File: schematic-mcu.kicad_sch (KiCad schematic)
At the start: 25 parts, among them U5 USBLC6-2P6, U6 ESP32-S3FN8, Y1 Crystal_GND24

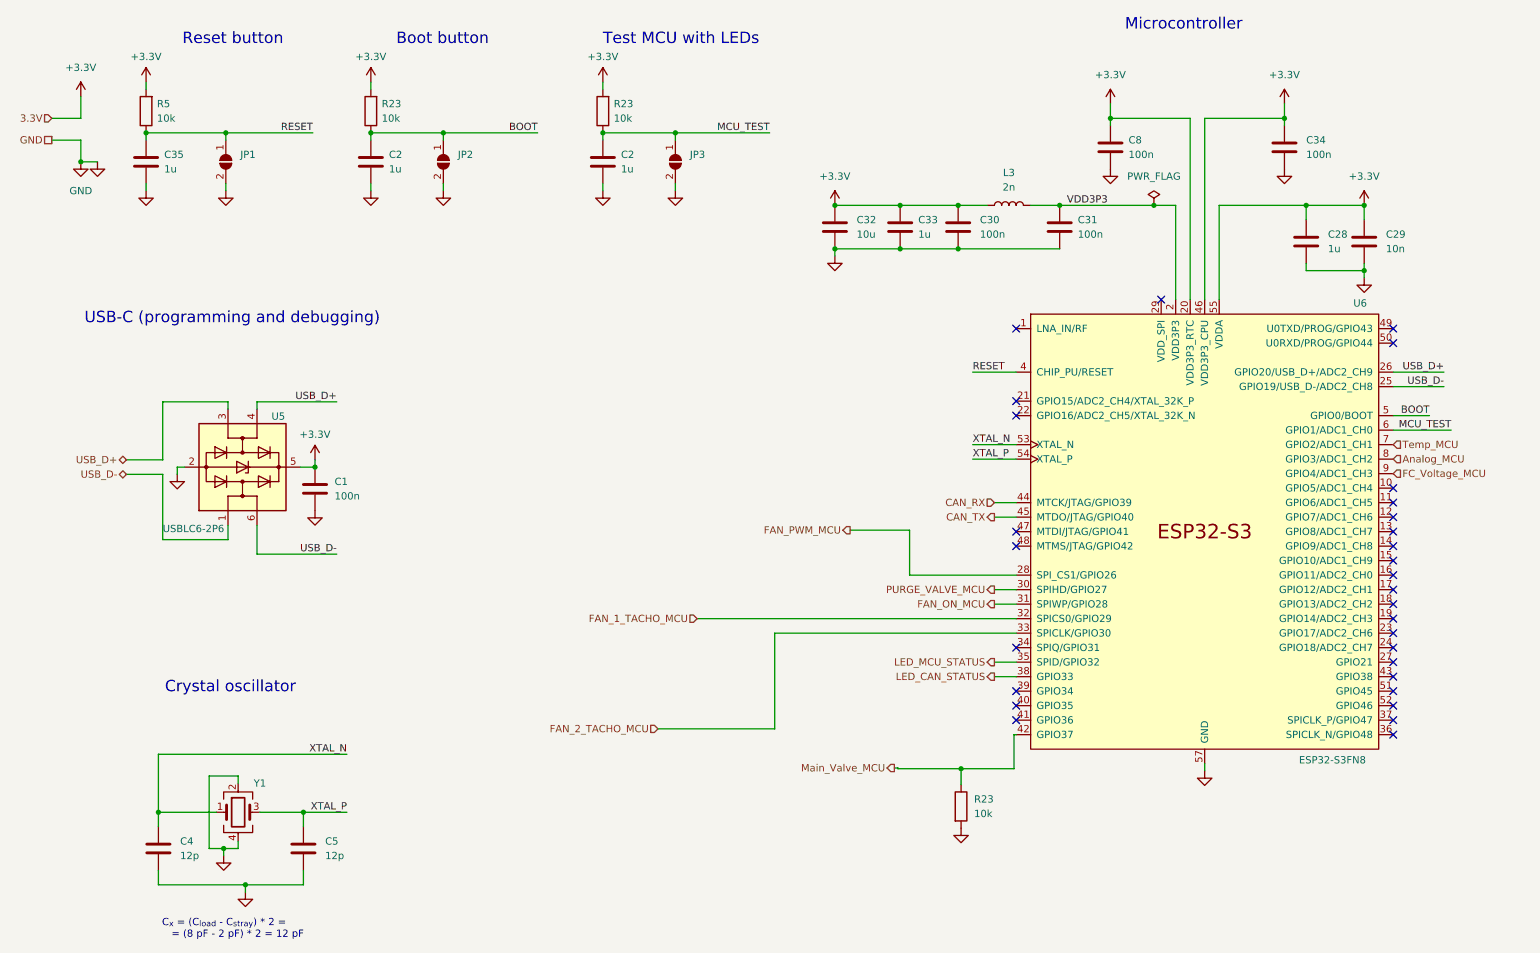
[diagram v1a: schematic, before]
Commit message: Edit mosfets outputs
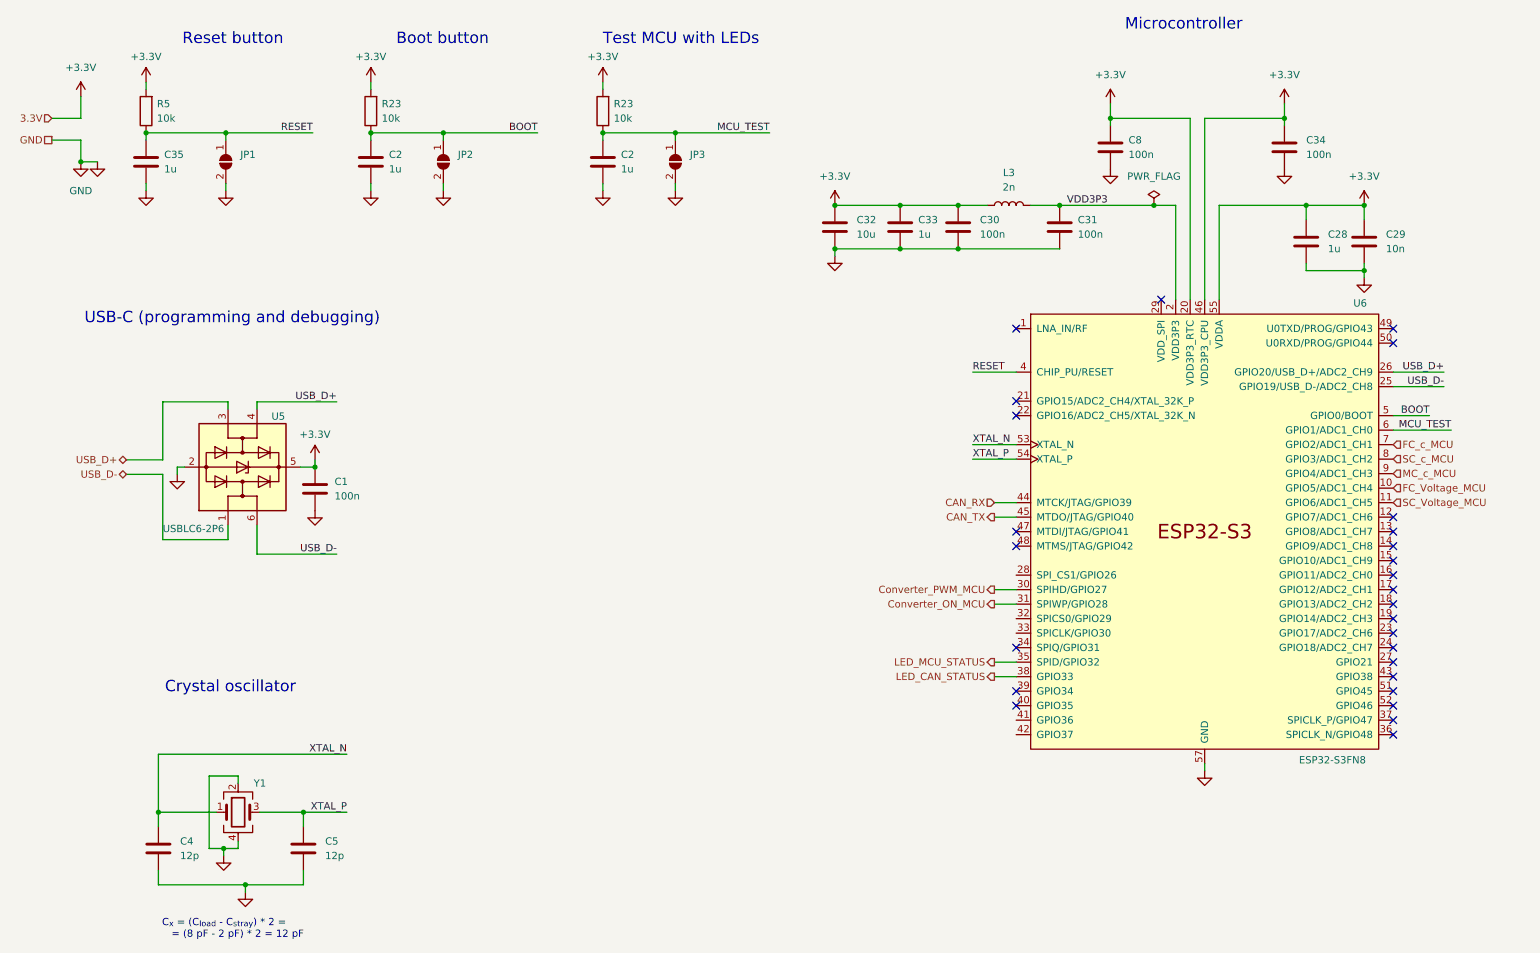
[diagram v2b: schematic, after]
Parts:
- removed R23: 10k, LED_SMD:LED_1206_3216Metric, symbol Device:R
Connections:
- net FC_Voltage_MCU: now also U6.10 (GPIO5/ADC1_CH4); no longer U6.9 (GPIO4/ADC1_CH3)
- net SC_Voltage_MCU: now reaches U6.11 (GPIO6/ADC1_CH5)
- net Analog_MCU renamed SC_c_MCU
- net FAN_1_TACHO_MCU: no longer names the net of U6.32 (SPICS0/GPIO29)
- net FAN_2_TACHO_MCU: no longer names the net of U6.33 (SPICLK/GPIO30)
- net FAN_ON_MCU renamed Converter_ON_MCU
- net FAN_PWM_MCU: no longer names the net of U6.28 (SPI_CS1/GPIO26)
- net Main_Valve_MCU: no longer names the net of U6.42 (GPIO37)
- net PURGE_VALVE_MCU renamed Converter_PWM_MCU
- net Temp_MCU renamed FC_c_MCU
- new net MC_c_MCU: U6.9 (GPIO4/ADC1_CH3)
- no-connect marks 30 -> 27
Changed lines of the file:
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@@
   (junction (at 185.42 53.34) (diameter 0) (color 0 0 0 0)
-  )
-  (junction (at 185.928 152.019) (diameter 0) (color 0 0 0 0)
   )
   (junction (at 31.75 45.72) (diameter 0) (color 0 0 0 0)
@@
   (no_connect (at 261.62 130.81))
   (no_connect (at 195.58 74.93))
-  (no_connect (at 261.62 102.87))
   (no_connect (at 195.58 138.43))
   (no_connect (at 261.62 118.11))
@@
   (no_connect (at 261.62 146.05))
   (no_connect (at 261.62 110.49))
-  (no_connect (at 195.58 143.51))
   (no_connect (at 195.58 110.49))
   (no_connect (at 261.62 135.89))
-  (no_connect (at 261.62 105.41))
   (wire (pts (xy 163.83 62.23) (xy 163.83 60.96))
     (stroke (width 0) (type default))
@@
     (stroke (width 0) (type default))
   )
-  (wire (pts (xy 185.928 152.019) (xy 195.199 152.019))
-    (stroke (width 0) (type default))
-  )
   (wire (pts (xy 270.51 82.55) (xy 261.62 82.55))
     (stroke (width 0) (type default))
@@
     (stroke (width 0) (type default))
   )
-  (wire (pts (xy 176.911 110.236) (xy 176.911 118.11))
-    (stroke (width 0) (type default))
-  )
   (wire (pts (xy 191.77 135.89) (xy 195.58 135.89))
     (stroke (width 0) (type default))
@@
     (stroke (width 0) (type default))
   )
-  (wire (pts (xy 195.199 152.019) (xy 195.199 146.05))
-    (stroke (width 0) (type default))
-  )
   (wire (pts (xy 212.09 38.1) (xy 226.06 38.1))
     (stroke (width 0) (type default))
@@
     (stroke (width 0) (type default))
   )
-  (wire (pts (xy 174.879 151.892) (xy 174.879 152.019))
-    (stroke (width 0) (type default))
-  )
   (wire (pts (xy 70.739 159.639) (xy 70.739 162.179))
     (stroke (width 0) (type default))
@@
     (stroke (width 0) (type default))
   )
-  (wire (pts (xy 166.497 110.236) (xy 176.911 110.236))
-    (stroke (width 0) (type default))
-  )
   (wire (pts (xy 203.2 53.34) (xy 219.71 53.34))
     (stroke (width 0) (type default))
@@
     (stroke (width 0) (type default))
   )
-  (wire (pts (xy 176.911 118.11) (xy 195.58 118.11))
-    (stroke (width 0) (type default))
-  )
   (wire (pts (xy 45.339 159.639) (xy 45.339 149.479))
     (stroke (width 0) (type default))
@@
     (stroke (width 0) (type default))
   )
-  (wire (pts (xy 153.289 145.034) (xy 153.289 128.27))
-    (stroke (width 0) (type default))
-  )
   (wire (pts (xy 55.499 159.639) (xy 45.339 159.639))
     (stroke (width 0) (type default))
@@
     (stroke (width 0) (type default))
   )
-  (wire (pts (xy 153.289 128.27) (xy 195.58 128.27))
-    (stroke (width 0) (type default))
-  )
   (wire (pts (xy 82.55 31.75) (xy 82.55 33.02))
     (stroke (width 0) (type default))
   )
-  (wire (pts (xy 132.842 145.034) (xy 153.289 145.034))
-    (stroke (width 0) (type default))
-  )
   (wire (pts (xy 82.55 40.64) (xy 95.25 40.64))
     (stroke (width 0) (type default))
@@
     (stroke (width 0) (type default))
   )
-  (wire (pts (xy 139.7 125.73) (xy 195.58 125.73))
-    (stroke (width 0) (type default))
-  )
   (wire (pts (xy 45.339 172.339) (xy 60.579 172.339))
     (stroke (width 0) (type default))
@@
     (stroke (width 0) (type default))
   )
-  (wire (pts (xy 174.879 151.892) (xy 174.244 151.892))
-    (stroke (width 0) (type default))
-  )
   (wire (pts (xy 226.06 38.1) (xy 226.06 69.85))
     (stroke (width 0) (type default))
@@
     (stroke (width 0) (type default))
   )
-  (wire (pts (xy 195.199 146.05) (xy 195.58 146.05))
-    (stroke (width 0) (type default))
-  )
   (wire (pts (xy 46.101 97.917) (xy 46.101 87.757))
     (stroke (width 0) (type default))
@@
     (stroke (width 0) (type default))
   )
-  (wire (pts (xy 174.879 152.019) (xy 185.928 152.019))
-    (stroke (width 0) (type default))
-  )
   (wire (pts (xy 54.229 165.989) (xy 56.769 165.989))
     (stroke (width 0) (type default))
   )
   (wire (pts (xy 123.19 50.8) (xy 123.19 49.53))
-    (stroke (width 0) (type default))
-  )
-  (wire (pts (xy 185.928 152.019) (xy 185.928 154.813))
     (stroke (width 0) (type default))
   )
@@
     (effects (font (size 1.27 1.27)) (justify right))
   )
-  (hierarchical_label "FAN_ON_MCU" (shape output) (at 191.77 123.19 180) (fields_autoplaced)
+  (hierarchical_label "Converter_ON_MCU" (shape output) (at 191.77 123.19 180) (fields_autoplaced)
     (effects (font (size 1.27 1.27)) (justify right))
   )
@@
     (effects (font (size 1.27 1.27)) (justify right))
   )
-  (hierarchical_label "Main_Valve_MCU" (shape output) (at 174.244 151.892 180) (fields_autoplaced)
-    (effects (font (size 1.27 1.27)) (justify right))
-  )
   (hierarchical_label "3.3V" (shape input) (at 26.67 38.1 180) (fields_autoplaced)
     (effects (font (size 1.27 1.27)) (justify right))
@@
     (effects (font (size 1.27 1.27)) (justify right))
   )
-  (hierarchical_label "Analog_MCU" (shape input) (at 261.62 97.79 0) (fields_autoplaced)
+  (hierarchical_label "SC_c_MCU" (shape input) (at 261.62 97.79 0) (fields_autoplaced)
     (effects (font (size 1.27 1.27)) (justify left))
   )
@@
     (effects (font (size 1.27 1.27)) (justify right))
   )
-  (hierarchical_label "FAN_1_TACHO_MCU" (shape input) (at 139.7 125.73 180) (fields_autoplaced)
+  (hierarchical_label "Converter_PWM_MCU" (shape output) (at 191.77 120.65 180) (fields_autoplaced)
     (effects (font (size 1.27 1.27)) (justify right))
   )
-  (hierarchical_label "PURGE_VALVE_MCU" (shape output) (at 191.77 120.65 180) (fields_autoplaced)
-    (effects (font (size 1.27 1.27)) (justify right))
-  )
-  (hierarchical_label "FAN_PWM_MCU" (shape output) (at 166.497 110.236 180) (fields_autoplaced)
-    (effects (font (size 1.27 1.27)) (justify right))
-  )
-  (hierarchical_label "FC_Voltage_MCU" (shape input) (at 261.62 100.33 0) (fields_autoplaced)
+  (hierarchical_label "MC_c_MCU" (shape input) (at 261.62 100.33 0) (fields_autoplaced)
     (effects (font (size 1.27 1.27)) (justify left))
   )
@@
     (effects (font (size 1.27 1.27)) (justify right))
   )
-  (hierarchical_label "FAN_2_TACHO_MCU" (shape input) (at 132.842 145.034 180) (fields_autoplaced)
-    (effects (font (size 1.27 1.27)) (justify right))
-  )
-  (hierarchical_label "Temp_MCU" (shape input) (at 261.62 95.25 0) (fields_autoplaced)
+  (hierarchical_label "FC_Voltage_MCU" (shape input) (at 261.62 102.87 0) (fields_autoplaced)
+    (effects (font (size 1.27 1.27)) (justify left))
+  )
+  (hierarchical_label "FC_c_MCU" (shape input) (at 261.62 95.25 0) (fields_autoplaced)
+    (effects (font (size 1.27 1.27)) (justify left))
+  )
+  (hierarchical_label "SC_Voltage_MCU" (shape input) (at 261.62 105.41 0) (fields_autoplaced)
     (effects (font (size 1.27 1.27)) (justify left))
   )
@@
         (path "/c9ad7189-d3b2-414a-9743-efd8e57cd755/f92f58ec-64e0-437c-bc00-8ae46a3b3054"
           (reference "C15") (unit 1)
-        )
-      )
-    )
-  )
-  (symbol (lib_id "power:GND") (at 185.928 162.433 0) (unit 1)
-    (in_bom yes) (on_board yes) (dnp no) (fields_autoplaced)
-    (property "Reference" "#PWR053" (at 185.928 168.783 0)
-      (effects (font (size 1.27 1.27)) hide)
-    )
-    (property "Value" "GND" (at 185.928 167.513 0)
-      (effects (font (size 1.27 1.27)) hide)
-    )
-    (property "Footprint" "" (at 185.928 162.433 0)
-      (effects (font (size 1.27 1.27)) hide)
-    )
-    (property "Datasheet" "" (at 185.928 162.433 0)
-      (effects (font (size 1.27 1.27)) hide)
-    )
-    (pin "1")
-    (instances
-      (project "schematic-main"
-        (path "/c9ad7189-d3b2-414a-9743-efd8e57cd755"
-          (reference "#PWR053") (unit 1)
-        )
-        (path "/c9ad7189-d3b2-414a-9743-efd8e57cd755/e4695f4d-6fa6-4597-a598-6a2f28a255eb"
-          (reference "#PWR047") (unit 1)
-        )
-        (path "/c9ad7189-d3b2-414a-9743-efd8e57cd755/f92f58ec-64e0-437c-bc00-8ae46a3b3054"
-          (reference "#PWR077") (unit 1)
         )
       )
@@
         )
       )
-    )
-  )
-  (symbol (lib_id "Device:R") (at 185.928 158.623 0) (unit 1)
-    (in_bom yes) (on_board yes) (dnp no) (fields_autoplaced)
-    (property "Reference" "R23" (at 188.214 157.353 0)
-      (effects (font (size 1.27 1.27)) (justify left))
-    )
-    (property "Value" "10k" (at 188.214 159.893 0)
-      (effects (font (size 1.27 1.27)) (justify left))
-    )
-    (property "Footprint" "LED_SMD:LED_1206_3216Metric" (at 184.15 158.623 90)
-      (effects (font (size 1.27 1.27)) hide)
-    )
-    (property "Datasheet" "~" (at 185.928 158.623 0)
-      (effects (font (size 1.27 1.27)) hide)
-    )
-    (pin "1")
-    (pin "2")
-    (instances
-      (project "schematic-main"
-        (path "/c9ad7189-d3b2-414a-9743-efd8e57cd755"
-          (reference "R23") (unit 1)
-        )
-        (path "/c9ad7189-d3b2-414a-9743-efd8e57cd755/f92f58ec-64e0-437c-bc00-8ae46a3b3054"
-          (reference "R47") (unit 1)
-        )
-      )

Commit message: First pcb
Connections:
- net I/O_1_MCU: now reaches U6.14 (GPIO9/ADC1_CH8)
- net I/O_2_MCU: now reaches U6.15 (GPIO10/ADC1_CH9)
- net I/O_3_MCU: now reaches U6.18 (GPIO13/ADC2_CH2)
- net I/O_4_MCU: now reaches U6.23 (GPIO17/ADC2_CH6)
- no-connect marks 27 -> 23

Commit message: Buck - boost converter
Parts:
- renumbered C35 to C13, C4 to C14, C5 to C15, C1 to C16, C2 to C17, C2 to C18, C32 to C19, C33 to C20, C30 to C21, C31 to C22, C8 to C23, C34 to C24, C28 to C25, C29 to C26, L3 to L2, R5 to R12, R23 to R13, R23 to R14, U5 to U2, U6 to U3
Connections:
- net Converter_PWM_B_MCU: now reaches U3.41 (GPIO36)
- net Converter_ON_B_MCU: now reaches U3.42 (GPIO37)
- net Converter_ON_MCU renamed Converter_ON_A_MCU
- net Converter_PWM_MCU renamed Converter_PWM_A_MCU

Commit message: Add pot
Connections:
- net SCL_D_Pot_i2c_MCU: now reaches U3.32 (SPICS0/GPIO29)
- net SDA_D_Pot_i2c_MCU: now reaches U3.33 (SPICLK/GPIO30)
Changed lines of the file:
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@@
+	(wire
+		(pts
+			(xy 190.119 125.73) (xy 195.58 125.73)
+		)
+		(stroke
+			(width 0)
+			(type default)
+		)
+	)
 	(wire
 		(pts
@@
 		(pts
 			(xy 43.18 40.64) (xy 57.15 40.64)
+		)
+		(stroke
+			(width 0)
+			(type default)
+		)
+	)
+	(wire
+		(pts
+			(xy 190.246 128.27) (xy 195.58 128.27)
 		)
 		(stroke
@@
 		)
 	)
+	(hierarchical_label "SCL_D_Pot_i2c_MCU"
+		(shape output)
+		(at 190.119 125.73 180)
+		(fields_autoplaced yes)
+		(effects
+			(font
+				(size 1.27 1.27)
+			)
+			(justify right)
+		)
+	)
 	(hierarchical_label "GND"
 		(shape passive)
@@
 		(fields_autoplaced yes)
 		(effects
+			(font
+				(size 1.27 1.27)
+			)
+			(justify right)
+		)
+	)
+	(hierarchical_label "SDA_D_Pot_i2c_MCU"
+		(shape output)
+		(at 190.246 128.27 180)
+		(fields_autoplaced yes)
+		(effects

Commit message: PCB design 50%
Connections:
- net FC_c_MCU: now also U3.14 (GPIO9/ADC1_CH8); no longer U3.7 (GPIO2/ADC1_CH1)
- net I/O_1_MCU: now also U3.12 (GPIO7/ADC1_CH6); no longer U3.14 (GPIO9/ADC1_CH8)
- net I/O_2_MCU: now also U3.13 (GPIO8/ADC1_CH7); no longer U3.15 (GPIO10/ADC1_CH9)
- net I/O_3_MCU: now also U3.16 (GPIO11/ADC2_CH0); no longer U3.18 (GPIO13/ADC2_CH2)
- net I/O_4_MCU: now also U3.18 (GPIO13/ADC2_CH2); no longer U3.23 (GPIO17/ADC2_CH6)
- net MC_c_MCU: now also U3.24 (GPIO18/ADC2_CH7); no longer U3.9 (GPIO4/ADC1_CH3)
- net SCL_D_Pot_i2c_MCU: now also U3.28 (SPI_CS1/GPIO26); no longer U3.32 (SPICS0/GPIO29)
- net SC_Voltage_MCU: now also U3.8 (GPIO3/ADC1_CH2); no longer U3.11 (GPIO6/ADC1_CH5)
- net SC_c_MCU: now also U3.23 (GPIO17/ADC2_CH6); no longer U3.8 (GPIO3/ADC1_CH2)
- net SDA_D_Pot_i2c_MCU: now also U3.27 (GPIO21); no longer U3.33 (SPICLK/GPIO30)
- no-connect marks 23 -> 24
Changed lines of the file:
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@@
 	)
 	(no_connect
-		(at 261.62 130.81)
+		(at 261.62 115.57)
 	)
 	(no_connect
@@
 	)
 	(no_connect
+		(at 195.58 125.73)
+	)
+	(no_connect
 		(at 195.58 138.43)
 	)
@@
 	)
 	(no_connect
-		(at 261.62 110.49)
+		(at 261.62 95.25)
 	)
 	(no_connect
@@
 	)
 	(no_connect
+		(at 261.62 100.33)
+	)
+	(no_connect
 		(at 195.58 130.81)
 	)
@@
 	)
 	(no_connect
-		(at 261.62 118.11)
-	)
-	(no_connect
-		(at 261.62 133.35)
-	)
-	(no_connect
 		(at 261.62 125.73)
 	)
@@
 	)
 	(no_connect
+		(at 261.62 105.41)
+	)
+	(no_connect
 		(at 261.62 146.05)
 	)
 	(no_connect
+		(at 195.58 128.27)
+	)
+	(no_connect
 		(at 195.58 110.49)
 	)
@@
 		(at 261.62 135.89)
 	)
-	(no_connect
-		(at 261.62 107.95)
-	)
 	(wire
 		(pts
@@
 	(wire
 		(pts
-			(xy 190.119 125.73) (xy 195.58 125.73)
-		)
-		(stroke
-			(width 0)
-			(type default)
-		)
-	)
-	(wire
-		(pts
 			(xy 191.77 107.95) (xy 195.58 107.95)
 		)
@@
 		(pts
 			(xy 43.18 40.64) (xy 57.15 40.64)
-		)
-		(stroke
-			(width 0)
-			(type default)
-		)
-	)
-	(wire
-		(pts
-			(xy 190.246 128.27) (xy 195.58 128.27)
 		)
 		(stroke
@@
 		)
 	)
-	(hierarchical_label "I{slash}O_2_MCU"
-		(shape input)
-		(at 261.62 115.57 0)
-		(fields_autoplaced yes)
-		(effects
-			(font
-				(size 1.27 1.27)
-			)
-			(justify left)
-		)
-	)
 	(hierarchical_label "CAN_RX"
 		(shape input)
@@
 		)
 	)
-	(hierarchical_label "SC_c_MCU"
+	(hierarchical_label "FC_c_MCU"
 		(shape input)
-		(at 261.62 97.79 0)
+		(at 261.62 113.03 0)
 		(fields_autoplaced yes)
 		(effects
@@
 	(hierarchical_label "SCL_D_Pot_i2c_MCU"
 		(shape output)
-		(at 190.119 125.73 180)
+		(at 195.58 118.11 180)
 		(fields_autoplaced yes)
 		(effects
@@
 			)
 			(justify right)
+		)
+	)
+	(hierarchical_label "I{slash}O_2_MCU"
+		(shape input)
+		(at 261.62 110.49 0)
+		(fields_autoplaced yes)
+		(effects
+			(font
+				(size 1.27 1.27)
+			)
+			(justify left)
 		)
 	)
@@
 		)
 	)
-	(hierarchical_label "I{slash}O_4_MCU"
-		(shape input)
-		(at 261.62 128.27 0)
-		(fields_autoplaced yes)
-		(effects
-			(font
-				(size 1.27 1.27)
-			)
-			(justify left)
-		)
-	)
 	(hierarchical_label "I{slash}O_1_MCU"
 		(shape input)
-		(at 261.62 113.03 0)
+		(at 261.62 107.95 0)
+		(fields_autoplaced yes)
+		(effects
+			(font
+				(size 1.27 1.27)
+			)
+			(justify left)
+		)
+	)
+	(hierarchical_label "SC_Voltage_MCU"
+		(shape input)
+		(at 261.62 97.79 0)
 		(fields_autoplaced yes)
 		(effects
@@
 		)
 	)
+	(hierarchical_label "I{slash}O_3_MCU"
+		(shape input)
+		(at 261.62 118.11 0)
+		(fields_autoplaced yes)
+		(effects
+			(font
+				(size 1.27 1.27)
+			)
+			(justify left)
+		)
+	)
 	(hierarchical_label "Converter_PWM_B_MCU"
 		(shape output)
@@
 		)
 	)
-	(hierarchical_label "MC_c_MCU"
+	(hierarchical_label "SC_c_MCU"
 		(shape input)
-		(at 261.62 100.33 0)
+		(at 261.62 128.27 0)
 		(fields_autoplaced yes)
 		(effects
@@
 		)
 	)
-	(hierarchical_label "SDA_D_Pot_i2c_MCU"
-		(shape output)
-		(at 190.246 128.27 180)
-		(fields_autoplaced yes)
-		(effects
-			(font
-				(size 1.27 1.27)
-			)
-			(justify right)
-		)
-	)
 	(hierarchical_label "FC_Voltage_MCU"
 		(shape input)
@@
 		)
 	)
-	(hierarchical_label "I{slash}O_3_MCU"
+	(hierarchical_label "SDA_D_Pot_i2c_MCU"
+		(shape output)
+		(at 261.62 133.35 0)
+		(fields_autoplaced yes)
+		(effects
+			(font
+				(size 1.27 1.27)
+			)
+			(justify left)
+		)
+	)
+	(hierarchical_label "I{slash}O_4_MCU"
 		(shape input)
 		(at 261.62 123.19 0)
-		(fields_autoplaced yes)
-		(effects
-			(font
-				(size 1.27 1.27)
-			)
-			(justify left)
-		)
-	)
-	(hierarchical_label "FC_c_MCU"
-		(shape input)
-		(at 261.62 95.25 0)
-		(fields_autoplaced yes)
-		(effects
-			(font
-				(size 1.27 1.27)
-			)
-			(justify left)
-		)
-	)
-	(hierarchical_label "SC_Voltage_MCU"
-		(shape input)
-		(at 261.62 105.41 0)
 		(fields_autoplaced yes)
 		(effects
@@
 		)
 	)
+	(hierarchical_label "MC_c_MCU"
+		(shape input)
+		(at 261.62 130.81 0)
+		(fields_autoplaced yes)
+		(effects
+			(font
+				(size 1.27 1.27)
+			)
+			(justify left)
+		)
+	)

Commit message: PCB design 80%
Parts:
- R14: footprint LED_SMD:LED_1206_3216Metric -> Resistor_SMD:R_1206_3216Metric
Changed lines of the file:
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@@
 			)
 		)
-		(property "Footprint" "LED_SMD:LED_1206_3216Metric"
+		(property "Footprint" "Resistor_SMD:R_1206_3216Metric"
 			(at 124.968 36.83 90)
 			(effects
